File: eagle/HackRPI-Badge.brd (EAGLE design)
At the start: 124.5 x 94 mm, 44 parts, among them J1 FTDI_BASICPTH, J2 SOLDERJUMPERTRACE-PTH, U2 3.3V, U4 74595, U5 74595, U6 74595, U7 74165DT, U8 AT25SF041

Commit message: Removed external flash memory from badge (ESP-12 module has plenty of flash onboard)
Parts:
- removed U8: AT25SF041, SparkFun-DigitalIC:SO08WIDE
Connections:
- removed net FLASH_CS: R3.1, U1.12, U8.1
- new net GPIO0: R3.1, U1.12
- net 3.3V: no longer U8.3, U8.7, U8.8
- net GND: no longer U8.4
- net MISO: no longer U8.2
- net MOSI: no longer U8.5
- net SCK: no longer U8.6
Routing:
- net FLASH_CS: track 62.8 -> 0.00 mm, vias 4 -> 0
- net GPIO0: track 0.00 -> 31.2 mm, vias 0 -> 2
- net MISO: track 77.9 -> 49.2 mm
- net 3.3V: track 305.7 -> 284.5 mm
- net SCK: track 147.4 -> 139.6 mm
- net MOSI: track 57.8 -> 55.0 mm
- net GND: track 38.3 -> 36.5 mm, vias 15 -> 14
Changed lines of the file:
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@@
 <attribute name="PARTNO" value="BK-82" x="116.84" y="45.72" size="1.778" layer="28" rot="MR270" display="off"/>
-</element>
-<element name="U8" library="SparkFun-DigitalIC" package="SO08WIDE" value="AT25SF041" x="91.44" y="54.61" rot="R90">
-<attribute name="PARTNO" value="AT25SF041-SSHD-T" x="91.44" y="54.61" size="1.778" layer="27" rot="R90" display="off"/>
 </element>
 <element name="U$1" library="mylib" package="HACKRPI-LOGO" value="" x="60.325" y="46.6725" rot="MR270"/>
@@
 <wire x1="54.61" y1="57.15" x2="54.61" y2="59.69" width="0.4064" layer="1"/>
 <wire x1="56.125" y1="61.205" x2="57.025" y2="61.205" width="0.4064" layer="1"/>
-<contactref element="U8" pad="6"/>
-<wire x1="87.5538" y1="55.245" x2="89.2175" y2="55.245" width="0.4064" layer="1"/>
-<wire x1="89.78" y1="61.205" x2="89.78" y2="55.8075" width="0.4064" layer="1"/>
-<wire x1="89.78" y1="55.8075" x2="89.2175" y2="55.245" width="0.4064" layer="1"/>
 <contactref element="U7" pad="2"/>
 <wire x1="56.125" y1="61.205" x2="54.61" y2="59.69" width="0.4064" layer="1"/>
@@
 <wire x1="91.7575" y1="73.9775" x2="96.52" y2="73.9775" width="0.4064" layer="16"/>
 <via x="96.52" y="73.9775" extent="1-16" drill="0.3048"/>
-<wire x1="96.52" y1="73.9775" x2="97.6875" y2="75.145" width="0.4064" layer="1"/>
-<wire x1="97.6875" y1="75.145" x2="100.45" y2="75.145" width="0.4064" layer="1"/>
-<contactref element="U8" pad="2"/>
-<wire x1="95.0087" y1="53.975" x2="97.155" y2="53.975" width="0.4064" layer="1"/>
-<wire x1="97.155" y1="53.975" x2="98.1075" y2="54.9275" width="0.4064" layer="1"/>
-<wire x1="98.1075" y1="54.9275" x2="98.1075" y2="62.5475" width="0.4064" layer="1"/>
-<wire x1="98.1075" y1="62.5475" x2="95.25" y2="65.405" width="0.4064" layer="1"/>
-<wire x1="95.25" y1="65.405" x2="95.25" y2="72.7075" width="0.4064" layer="1"/>
-<wire x1="95.25" y1="72.7075" x2="96.52" y2="73.9775" width="0.4064" layer="1"/>
+<wire x1="96.52" y1="73.9775" x2="100.45" y2="75.145" width="0" layer="19" extent="1-1"/>
 </signal>
 <signal name="MOSI">
@@
 <via x="97.5925" y="73.145" extent="1-16" drill="0.3048"/>
 <wire x1="97.5925" y1="73.145" x2="92.83" y2="73.145" width="0.4064" layer="16"/>
-<contactref element="U8" pad="5"/>
-<wire x1="87.5538" y1="59.2963" x2="87.5538" y2="56.515" width="0.4064" layer="1"/>
 <wire x1="88.265" y1="63.5" x2="88.265" y2="60.0075" width="0.4064" layer="16"/>
 <via x="88.265" y="60.0075" extent="1-16" drill="0.3048"/>
@@
 <wire x1="57.025" y1="60.555" x2="61.365" y2="60.555" width="0.508" layer="1"/>
 <wire x1="61.365" y1="60.555" x2="62.865" y2="59.055" width="0.508" layer="1"/>
-<contactref element="U8" pad="3"/>
-<contactref element="U8" pad="8"/>
-<contactref element="U8" pad="7"/>
-<wire x1="87.5538" y1="52.705" x2="87.5538" y2="53.975" width="0.6096" layer="1"/>
-<wire x1="87.5538" y1="53.975" x2="90.805" y2="53.975" width="0.6096" layer="1"/>
-<wire x1="95.0087" y1="55.245" x2="92.075" y2="55.245" width="0.6096" layer="1"/>
-<wire x1="92.075" y1="55.245" x2="90.805" y2="53.975" width="0.6096" layer="1"/>
-<wire x1="90.805" y1="53.975" x2="90.805" y2="52.3875" width="0.6096" layer="1"/>
-<wire x1="90.805" y1="52.3875" x2="92.3925" y2="50.8" width="0.6096" layer="1"/>
-<wire x1="100.45" y1="50.8" x2="92.3925" y2="50.8" width="0.6096" layer="1"/>
 <wire x1="100.45" y1="50.8" x2="100.45" y2="50.4825" width="0.6096" layer="1"/>
 </signal>
@@
 <wire x1="48.26" y1="57.58" x2="48.26" y2="53.34" width="0.508" layer="1"/>
 <via x="48.26" y="53.34" extent="1-16" drill="0.3048"/>
-<contactref element="U8" pad="4"/>
-<wire x1="95.0087" y1="56.515" x2="96.8375" y2="56.515" width="0.6096" layer="1"/>
-<via x="96.8375" y="56.515" extent="1-16" drill="0.3048"/>
 <wire x1="99.96" y1="22.86" x2="101.6" y2="22.86" width="1.27" layer="1"/>
 <wire x1="93.715" y1="20.0025" x2="92.075" y2="20.0025" width="1.27" layer="1"/>
@@
 <wire x1="55.55" y1="74.9175" x2="55.55" y2="73.15" width="0.4064" layer="1"/>
 </signal>
-<signal name="FLASH_CS">
+<signal name="GPIO0">
 <contactref element="U1" pad="12"/>
 <contactref element="R3" pad="1"/>
@@
 <wire x1="119.165" y1="77.47" x2="118.84" y2="77.145" width="0.8128" layer="1"/>
 <wire x1="118.84" y1="77.145" x2="115.45" y2="77.145" width="0.8128" layer="1"/>
-<contactref element="U8" pad="1"/>
 <wire x1="95.25" y1="75.8825" x2="96.2025" y2="75.8825" width="0.4064" layer="16"/>
-<wire x1="95.0087" y1="52.705" x2="98.425" y2="52.705" width="0.4064" layer="1"/>
-<via x="98.425" y="52.705" extent="1-16" drill="0.3048"/>
-<wire x1="98.425" y1="52.705" x2="102.5525" y2="52.705" width="0.4064" layer="16"/>
-<wire x1="102.5525" y1="52.705" x2="103.1875" y2="53.34" width="0.4064" layer="16"/>
-<wire x1="103.1875" y1="53.34" x2="103.1875" y2="65.0875" width="0.4064" layer="16"/>
-<via x="103.1875" y="65.0875" extent="1-16" drill="0.3048"/>
-<wire x1="103.1875" y1="65.0875" x2="103.1875" y2="69.215" width="0.4064" layer="1"/>
-<wire x1="103.1875" y1="69.215" x2="104.775" y2="70.8025" width="0.4064" layer="1"/>
-<wire x1="104.775" y1="70.8025" x2="104.775" y2="75.8825" width="0.4064" layer="1"/>
 </signal>
 <signal name="V_BATT" class="1">

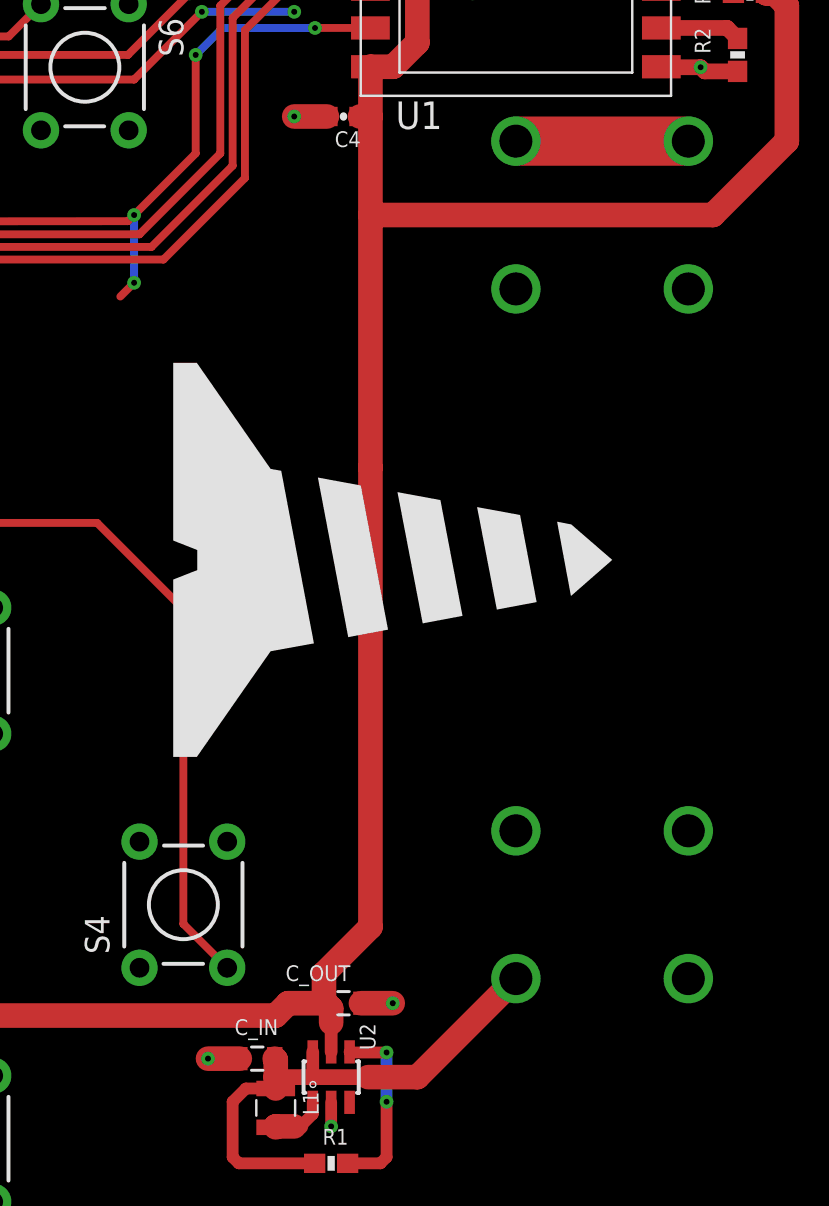
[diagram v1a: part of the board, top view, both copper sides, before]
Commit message: Moved batteries away from eachother
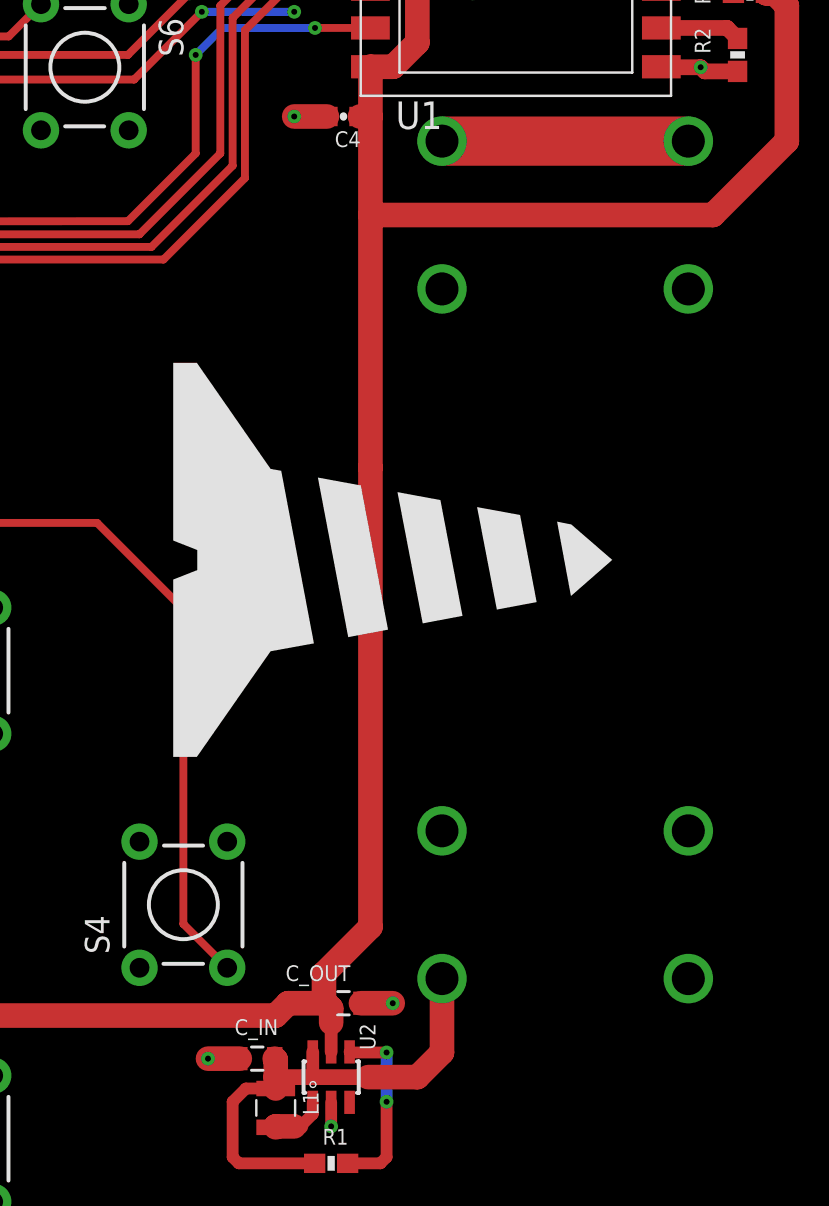
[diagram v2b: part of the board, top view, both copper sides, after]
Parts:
- moved BAT1 3.81 mm to (104.1, 45.7)
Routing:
- net MOSI: track 55.0 -> 50.5 mm, vias 4 -> 2
- net N$31: track 8.89 -> 12.7 mm
- net V_BATT: track 27.1 -> 25.5 mm
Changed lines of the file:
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@@
 <attribute name="PARTNO" value="CC0603ZRY5V9BB104" x="59.055" y="52.705" size="1.778" layer="27" rot="R90" display="off"/>
 </element>
-<element name="BAT1" library="SparkFun-Electromechanical" package="BATTERY-AAA" value="" x="107.95" y="45.72" rot="MR90">
-<attribute name="PROD_ID" value="BATT-08571" x="107.95" y="45.72" size="1.778" layer="28" rot="MR90" display="off"/>
-<attribute name="PARTNO" value="BK-82" x="107.95" y="45.72" size="1.778" layer="28" rot="MR90" display="off"/>
+<element name="BAT1" library="SparkFun-Electromechanical" package="BATTERY-AAA" value="" x="104.14" y="45.72" rot="MR90">
+<attribute name="PROD_ID" value="BATT-08571" x="104.14" y="45.72" size="1.778" layer="28" rot="MR90" display="off"/>
+<attribute name="PARTNO" value="BK-82" x="104.14" y="45.72" size="1.778" layer="28" rot="MR90" display="off"/>
 </element>
 <element name="BAT2" library="SparkFun-Electromechanical" package="BATTERY-AAA" value="" x="116.84" y="45.72" rot="MR270">
@@
 <contactref element="U6" pad="14"/>
 <wire x1="57.025" y1="63.155" x2="87.9475" y2="63.1825" width="0.4064" layer="1"/>
-<wire x1="87.9475" y1="63.1825" x2="88.265" y2="63.5" width="0.4064" layer="1"/>
-<wire x1="88.265" y1="63.5" x2="91.44" y2="66.675" width="0.4064" layer="1"/>
+<wire x1="87.9475" y1="63.1825" x2="91.44" y2="66.675" width="0.4064" layer="1"/>
 <wire x1="91.44" y1="66.675" x2="91.44" y2="71.755" width="0.4064" layer="1"/>
 <via x="91.44" y="71.755" extent="1-16" drill="0.3048"/>
@@
 <via x="97.5925" y="73.145" extent="1-16" drill="0.3048"/>
 <wire x1="97.5925" y1="73.145" x2="92.83" y2="73.145" width="0.4064" layer="16"/>
-<wire x1="88.265" y1="63.5" x2="88.265" y2="60.0075" width="0.4064" layer="16"/>
-<via x="88.265" y="60.0075" extent="1-16" drill="0.3048"/>
-<wire x1="88.265" y1="60.0075" x2="87.5538" y2="59.2963" width="0.4064" layer="1"/>
-<via x="88.265" y="63.5" extent="1-16" drill="0.3048"/>
 </signal>
 <signal name="3.3V" class="1">
@@
 <contactref element="U2" pad="6"/>
 <contactref element="BAT1" pad="PWR@1"/>
-<wire x1="102.87" y1="19.05" x2="107.95" y2="24.13" width="1.27" layer="1"/>
+<wire x1="102.87" y1="19.05" x2="104.14" y2="20.32" width="1.27" layer="1"/>
+<wire x1="104.14" y1="20.32" x2="104.14" y2="24.13" width="1.27" layer="1"/>
 <wire x1="95.515" y1="20.0025" x2="95.5675" y2="19.95" width="1.27" layer="1"/>
 <wire x1="95.5675" y1="19.95" x2="95.5675" y2="19.05" width="1.27" layer="1"/>
@@
 <contactref element="BAT2" pad="PWR@1"/>
 <contactref element="BAT1" pad="GND@1"/>
-<wire x1="107.95" y1="67.31" x2="116.84" y2="67.31" width="2.54" layer="1"/>
+<wire x1="104.14" y1="67.31" x2="116.84" y2="67.31" width="2.54" layer="1"/>
 </signal>
 <signal name="N$33">

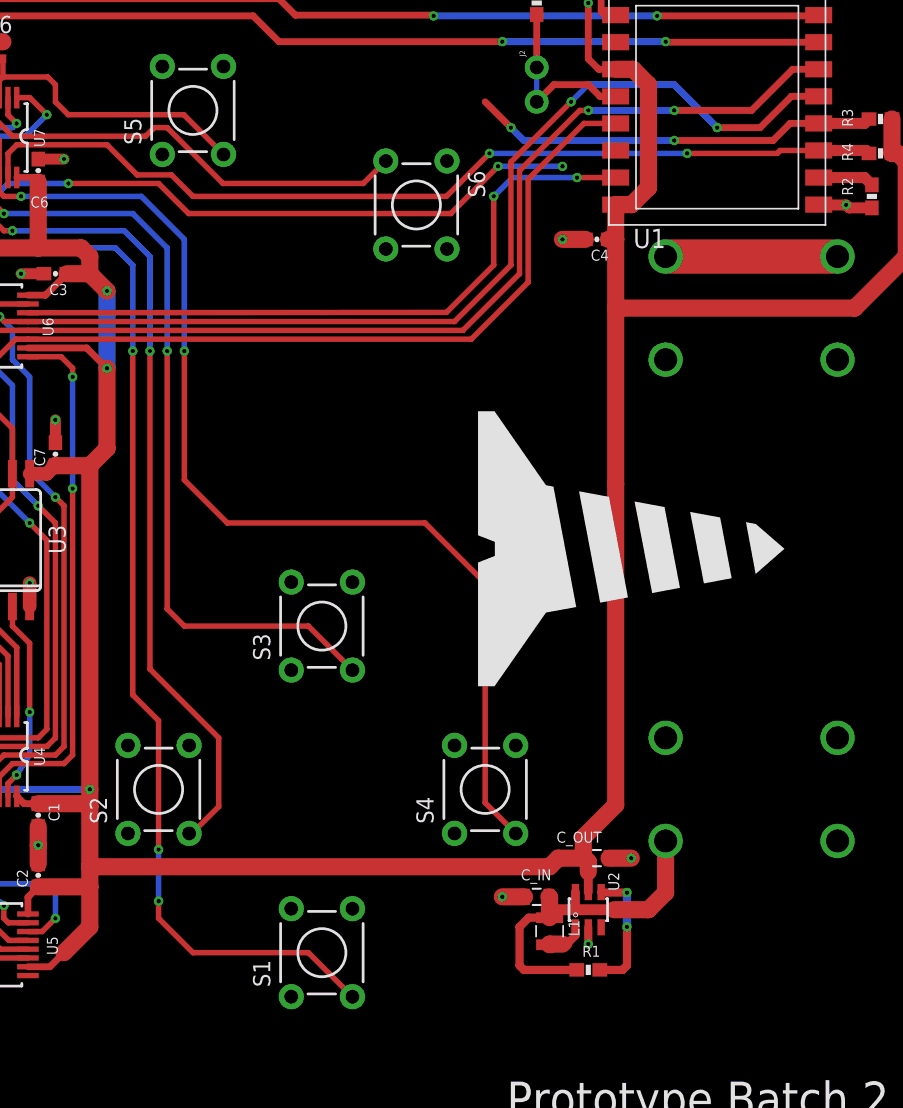
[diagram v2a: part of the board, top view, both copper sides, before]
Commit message: Moved buttons, changed some pin assignments, added input shift register source
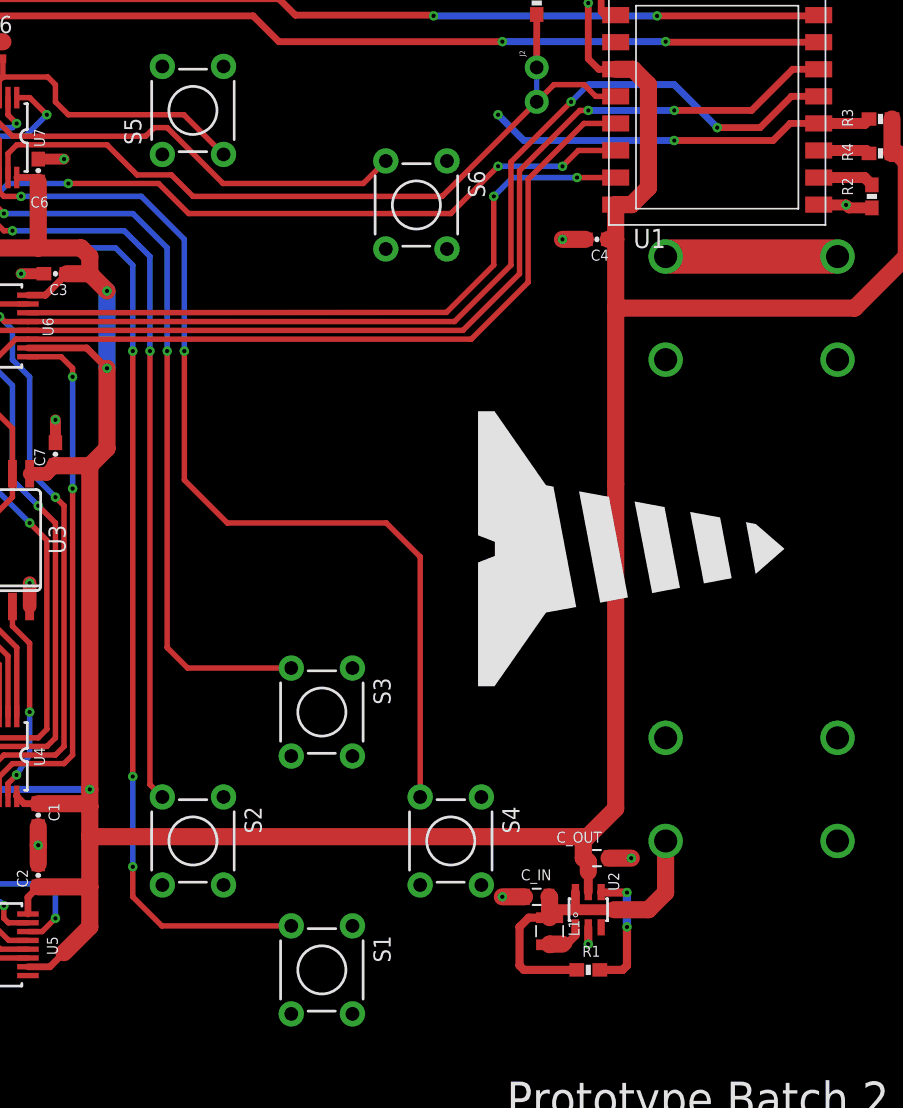
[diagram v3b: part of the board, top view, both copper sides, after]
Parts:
- C5: value .1uF -> 1uF
- moved S3 6.35 mm to (78.7, 33.7), turned to 270 degrees
- moved S2 4.58 mm to (69.2, 24.1), turned to 270 degrees
- moved S4 4.58 mm to (88.3, 24.1), turned to 270 degrees
- moved S1 1.27 mm to (78.7, 14.6), turned to 270 degrees
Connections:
- removed net GPIO16: J2.2, U1.4
- new net GPIO2: R4.1, U1.11
- net INPUT_CS: now also J2.2, U1.4; no longer R4.1, U1.11
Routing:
- net INPUT_CS: track 68.7 -> 52.3 mm, vias 2 -> 0
- net DOWN: track 88.9 -> 81.6 mm
- net GPIO16: track 6.72 -> 0.00 mm
- net LEFT: track 88.0 -> 81.5 mm
- net UP: track 69.3 -> 63.8 mm
- net MISO: track 49.2 -> 53.6 mm
- net GPIO2: track 0.00 -> 3.80 mm
- net RIGHT: track 67.1 -> 64.2 mm
- net GPIO0: track 31.2 -> 29.8 mm
